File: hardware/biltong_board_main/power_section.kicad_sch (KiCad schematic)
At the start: 17 parts, among them U3 TPS562202SDRLR

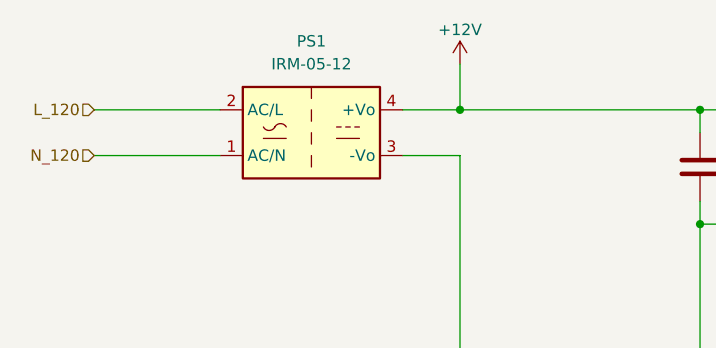
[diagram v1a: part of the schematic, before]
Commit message: generated BOM, swapped 10u cap size, README.md changes
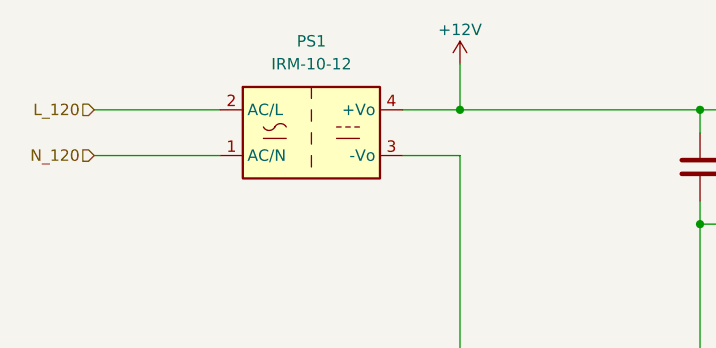
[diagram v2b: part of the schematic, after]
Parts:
- removed PS1: IRM-05-12, BiltongBoardLib:Converter_ACDC_MeanWell_IRM-05-xx_THT_w_model, symbol Converter_ACDC:IRM-05-12
- added PS1: IRM-10-12, BiltongBoardLib:Converter_ACDC_MeanWell_IRM-10-xx_THT_w_model, symbol Converter_ACDC:IRM-10-12
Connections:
- net +12V: now also PS1.4 (+Vo)
- net GND: now also PS1.3 (-Vo)
- net L_120: now also PS1.2 (AC/L)
- net N_120: now also PS1.1 (AC/N)
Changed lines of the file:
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@@
       (effects (font (size 1.27 1.27)) hide)
     )
-    (property "Datasheet" "~" (at 196.85 122.555 0)
+    (property "Datasheet" "https://www.digikey.com/en/products/detail/w%C3%BCrth-elektronik/150060VS75000/4489906" (at 196.85 122.555 0)
       (effects (font (size 1.27 1.27)) hide)
     )
@@
         (path "/0a1e579b-8207-4868-883c-1f24490f13ce/7102a496-acc8-417b-bbc2-3ab3ed47e45b"
           (reference "C19") (unit 1)
+        )
+      )
+    )
+  )
+  (symbol (lib_id "Converter_ACDC:IRM-10-12") (at 50.8 33.02 0) (unit 1)
+    (in_bom yes) (on_board yes) (dnp no) (fields_autoplaced)
+    (property "Reference" "PS1" (at 50.8 22.86 0)
+      (effects (font (size 1.27 1.27)))
+    )
+    (property "Value" "IRM-10-12" (at 50.8 25.4 0)
+      (effects (font (size 1.27 1.27)))
+    )
+    (property "Footprint" "BiltongBoardLib:Converter_ACDC_MeanWell_IRM-10-xx_THT_w_model" (at 50.8 41.91 0)
+      (effects (font (size 1.27 1.27)) hide)
+    )
+    (property "Datasheet" "https://www.meanwell.com/Upload/PDF/IRM-10/IRM-10-SPEC.PDF" (at 50.8 43.18 0)
+      (effects (font (size 1.27 1.27)) hide)
+    )
+    (pin "1")
+    (pin "2")
+    (pin "3")
+    (pin "4")
+    (instances
+      (project "biltong_board_main"
+        (path "/0a1e579b-8207-4868-883c-1f24490f13ce/7102a496-acc8-417b-bbc2-3ab3ed47e45b"
+          (reference "PS1") (unit 1)
         )
       )
@@
         )
       )
-    )
-  )
-  (symbol (lib_id "Converter_ACDC:IRM-05-12") (at 50.8 33.02 0) (unit 1)
-    (in_bom yes) (on_board yes) (dnp no) (fields_autoplaced)
-    (property "Reference" "PS1" (at 50.8 22.86 0)
-      (effects (font (size 1.27 1.27)))
-    )
-    (property "Value" "IRM-05-12" (at 50.8 25.4 0)
-      (effects (font (size 1.27 1.27)))
-    )
-    (property "Footprint" "BiltongBoardLib:Converter_ACDC_MeanWell_IRM-05-xx_THT_w_model" (at 50.8 41.91 0)
-      (effects (font (size 1.27 1.27)) hide)
-    )
-    (property "Datasheet" "https://www.meanwell.com/Upload/PDF/IRM-05/IRM-05-SPEC.PDF" (at 50.8 43.18 0)
-      (effects (font (size 1.27 1.27)) hide)
-    )
-    (pin "1")
-    (pin "2")
-    (pin "3")
-    (pin "4")
-    (instances
-      (project "biltong_board_main"
-        (path "/0a1e579b-8207-4868-883c-1f24490f13ce/7102a496-acc8-417b-bbc2-3ab3ed47e45b"
-          (reference "PS1") (unit 1)
-        )
-      )

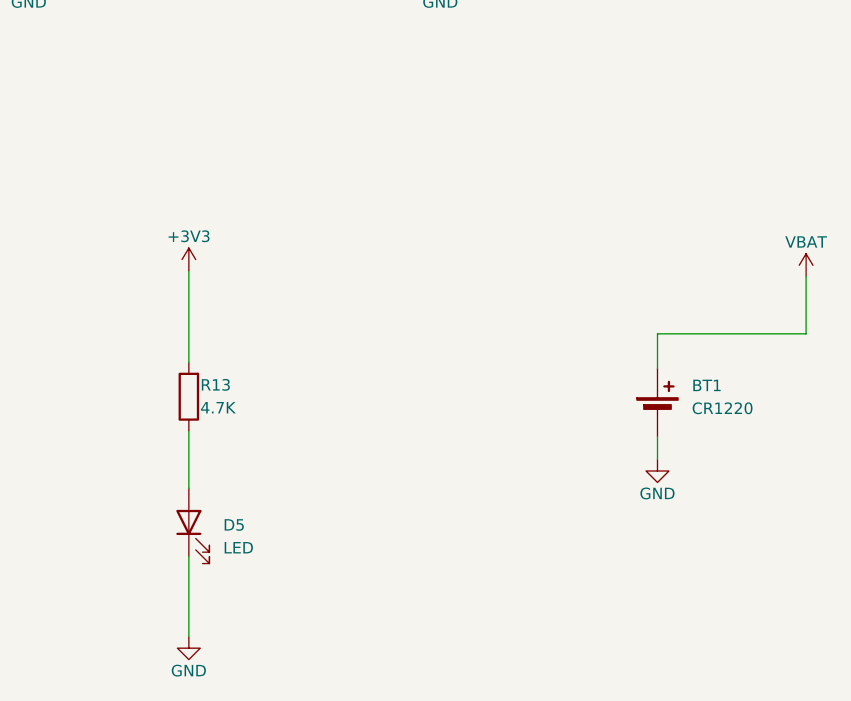
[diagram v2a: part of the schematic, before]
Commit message: Fixed HS1 ground issue, missing schematic values, README.md update
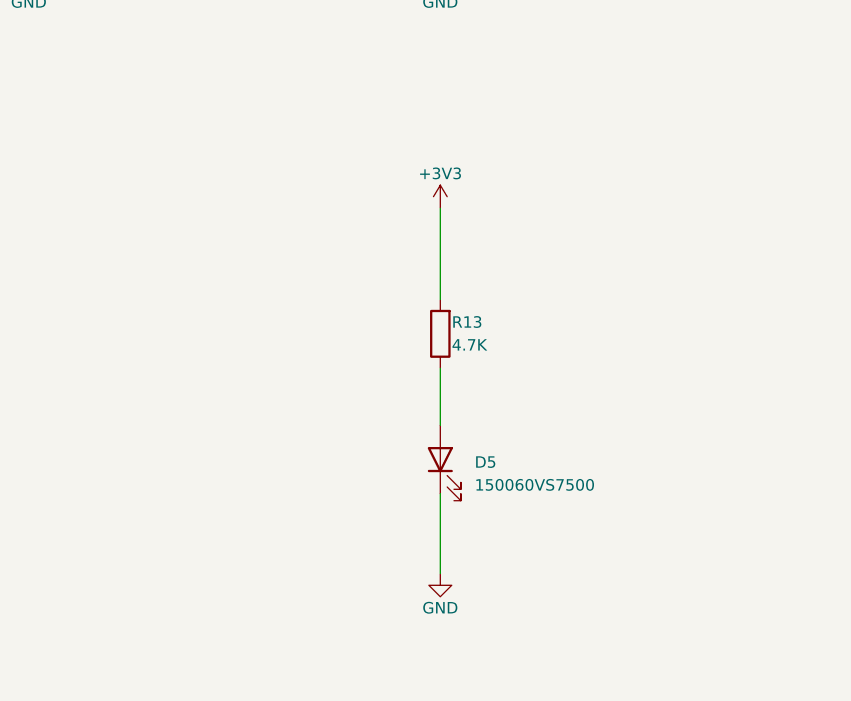
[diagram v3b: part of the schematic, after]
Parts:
- removed BT1: CR1220, BiltongBoardLib:BH-98-1, symbol Device:Battery_Cell
- D5: value LED -> 150060VS7500
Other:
- moved on the sheet: D5, R13
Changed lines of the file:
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@@
   (junction (at 224.79 30.48) (diameter 0) (color 0 0 0 0)
   )
-  (wire (pts (xy 196.85 126.365) (xy 196.85 135.255))
+  (wire (pts (xy 224.79 119.38) (xy 224.79 128.27))
     (stroke (width 0) (type default))
   )
@@
     (stroke (width 0) (type default))
   )
-  (wire (pts (xy 248.92 105.41) (xy 248.92 101.6))
-    (stroke (width 0) (type default))
-  )
   (wire (pts (xy 93.98 40.64) (xy 93.98 43.18))
     (stroke (width 0) (type default))
@@
     (stroke (width 0) (type default))
   )
-  (wire (pts (xy 248.92 113.03) (xy 248.92 115.57))
-    (stroke (width 0) (type default))
-  )
   (wire (pts (xy 203.2 60.96) (xy 195.58 60.96))
     (stroke (width 0) (type default))
@@
     (stroke (width 0) (type default))
   )
-  (wire (pts (xy 265.43 101.6) (xy 265.43 95.25))
-    (stroke (width 0) (type default))
-  )
-  (wire (pts (xy 196.85 112.395) (xy 196.85 118.745))
+  (wire (pts (xy 224.79 105.41) (xy 224.79 111.76))
     (stroke (width 0) (type default))
   )
@@
     (stroke (width 0) (type default))
   )
-  (wire (pts (xy 248.92 101.6) (xy 265.43 101.6))
-    (stroke (width 0) (type default))
-  )
-  (wire (pts (xy 196.85 94.615) (xy 196.85 104.775))
+  (wire (pts (xy 224.79 87.63) (xy 224.79 97.79))
     (stroke (width 0) (type default))
   )
@@
     )
   )
-  (symbol (lib_id "Device:LED") (at 196.85 122.555 90) (unit 1)
+  (symbol (lib_id "Device:LED") (at 224.79 115.57 90) (unit 1)
     (in_bom yes) (on_board yes) (dnp no) (fields_autoplaced)
-    (property "Reference" "D5" (at 200.66 122.8725 90)
+    (property "Reference" "D5" (at 228.6 115.8875 90)
       (effects (font (size 1.27 1.27)) (justify right))
     )
-    (property "Value" "LED" (at 200.66 125.4125 90)
+    (property "Value" "150060VS7500" (at 228.6 118.4275 90)
       (effects (font (size 1.27 1.27)) (justify right))
     )
-    (property "Footprint" "LED_SMD:LED_0603_1608Metric" (at 196.85 122.555 0)
-      (effects (font (size 1.27 1.27)) hide)
-    )
-    (property "Datasheet" "https://www.digikey.com/en/products/detail/w%C3%BCrth-elektronik/150060VS75000/4489906" (at 196.85 122.555 0)
+    (property "Footprint" "LED_SMD:LED_0603_1608Metric" (at 224.79 115.57 0)
+      (effects (font (size 1.27 1.27)) hide)
+    )
+    (property "Datasheet" "https://www.digikey.com/en/products/detail/w%C3%BCrth-elektronik/150060VS75000/4489906" (at 224.79 115.57 0)
       (effects (font (size 1.27 1.27)) hide)
     )
@@
     )
   )
-  (symbol (lib_id "BiltongBoard:VBAT") (at 265.43 95.25 0) (unit 1)
-    (in_bom yes) (on_board yes) (dnp no)
-    (property "Reference" "#PWR048" (at 265.43 87.63 0)
-      (effects (font (size 1.27 1.27)) hide)
-    )
-    (property "Value" "VBAT" (at 265.43 91.44 0)
-      (effects (font (size 1.27 1.27)))
-    )
-    (property "Footprint" "" (at 265.43 95.25 0)
-      (effects (font (size 1.27 1.27)) hide)
-    )
-    (property "Datasheet" "" (at 265.43 95.25 0)
-      (effects (font (size 1.27 1.27)) hide)
-    )
-    (pin "1")
-    (instances
-      (project "biltong_board_main"
-        (path "/0a1e579b-8207-4868-883c-1f24490f13ce/7102a496-acc8-417b-bbc2-3ab3ed47e45b"
-          (reference "#PWR048") (unit 1)
-        )
-      )
-    )
-  )
   (symbol (lib_id "Device:C") (at 207.01 60.96 90) (unit 1)
     (in_bom yes) (on_board yes) (dnp no)
@@
     )
   )
-  (symbol (lib_id "power:+3V3") (at 196.85 94.615 0) (mirror y) (unit 1)
-    (in_bom yes) (on_board yes) (dnp no)
-    (property "Reference" "#PWR032" (at 196.85 98.425 0)
-      (effects (font (size 1.27 1.27)) hide)
-    )
-    (property "Value" "+3V3" (at 196.85 90.805 0)
-      (effects (font (size 1.27 1.27)))
-    )
-    (property "Footprint" "" (at 196.85 94.615 0)
-      (effects (font (size 1.27 1.27)) hide)
-    )
-    (property "Datasheet" "" (at 196.85 94.615 0)
+  (symbol (lib_id "power:+3V3") (at 224.79 87.63 0) (mirror y) (unit 1)
+    (in_bom yes) (on_board yes) (dnp no)
+    (property "Reference" "#PWR032" (at 224.79 91.44 0)
+      (effects (font (size 1.27 1.27)) hide)
+    )
+    (property "Value" "+3V3" (at 224.79 83.82 0)
+      (effects (font (size 1.27 1.27)))
+    )
+    (property "Footprint" "" (at 224.79 87.63 0)
+      (effects (font (size 1.27 1.27)) hide)
+    )
+    (property "Datasheet" "" (at 224.79 87.63 0)
       (effects (font (size 1.27 1.27)) hide)
     )
@@
     )
   )
-  (symbol (lib_id "power:GND") (at 196.85 135.255 0) (mirror y) (unit 1)
-    (in_bom yes) (on_board yes) (dnp no)
-    (property "Reference" "#PWR033" (at 196.85 141.605 0)
-      (effects (font (size 1.27 1.27)) hide)
-    )
-    (property "Value" "GND" (at 196.85 139.065 0)
-      (effects (font (size 1.27 1.27)))
-    )
-    (property "Footprint" "" (at 196.85 135.255 0)
-      (effects (font (size 1.27 1.27)) hide)
-    )
-    (property "Datasheet" "" (at 196.85 135.255 0)
+  (symbol (lib_id "power:GND") (at 224.79 128.27 0) (mirror y) (unit 1)
+    (in_bom yes) (on_board yes) (dnp no)
+    (property "Reference" "#PWR033" (at 224.79 134.62 0)
+      (effects (font (size 1.27 1.27)) hide)
+    )
+    (property "Value" "GND" (at 224.79 132.08 0)
+      (effects (font (size 1.27 1.27)))
+    )
+    (property "Footprint" "" (at 224.79 128.27 0)
+      (effects (font (size 1.27 1.27)) hide)
+    )
+    (property "Datasheet" "" (at 224.79 128.27 0)
       (effects (font (size 1.27 1.27)) hide)
     )
@@
     )
   )
-  (symbol (lib_id "Device:R") (at 196.85 108.585 180) (unit 1)
-    (in_bom yes) (on_board yes) (dnp no)
-    (property "Reference" "R13" (at 198.12 107.315 0)
+  (symbol (lib_id "Device:R") (at 224.79 101.6 180) (unit 1)
+    (in_bom yes) (on_board yes) (dnp no)
+    (property "Reference" "R13" (at 226.06 100.33 0)
       (effects (font (size 1.27 1.27)) (justify right))
     )
-    (property "Value" "4.7K" (at 198.12 109.855 0)
+    (property "Value" "4.7K" (at 226.06 102.87 0)
       (effects (font (size 1.27 1.27)) (justify right))
     )
-    (property "Footprint" "Resistor_SMD:R_0603_1608Metric" (at 198.628 108.585 90)
-      (effects (font (size 1.27 1.27)) hide)
-    )
-    (property "Datasheet" "~" (at 196.85 108.585 0)
+    (property "Footprint" "Resistor_SMD:R_0603_1608Metric" (at 226.568 101.6 90)
+      (effects (font (size 1.27 1.27)) hide)
+    )
+    (property "Datasheet" "~" (at 224.79 101.6 0)
       (effects (font (size 1.27 1.27)) hide)
     )
@@
     )
   )
-  (symbol (lib_id "power:GND") (at 248.92 115.57 0) (unit 1)
-    (in_bom yes) (on_board yes) (dnp no)
-    (property "Reference" "#PWR012" (at 248.92 121.92 0)
-      (effects (font (size 1.27 1.27)) hide)
-    )
-    (property "Value" "GND" (at 248.92 119.38 0)
-      (effects (font (size 1.27 1.27)))
-    )
-    (property "Footprint" "" (at 248.92 115.57 0)
-      (effects (font (size 1.27 1.27)) hide)
-    )
-    (property "Datasheet" "" (at 248.92 115.57 0)
-      (effects (font (size 1.27 1.27)) hide)
-    )
-    (pin "1")
-    (instances
-      (project "biltong_board_main"
-        (path "/0a1e579b-8207-4868-883c-1f24490f13ce"
-          (reference "#PWR012") (unit 1)
-        )
-        (path "/0a1e579b-8207-4868-883c-1f24490f13ce/7102a496-acc8-417b-bbc2-3ab3ed47e45b"
-          (reference "#PWR031") (unit 1)
-        )
-      )
-    )
-  )
   (symbol (lib_id "power:+3V3") (at 265.43 25.4 0) (unit 1)
     (in_bom yes) (on_board yes) (dnp no)
@@
         )
       )
-    )
-  )
-  (symbol (lib_id "Device:Battery_Cell") (at 248.92 110.49 0) (unit 1)
-    (in_bom yes) (on_board yes) (dnp no) (fields_autoplaced)
-    (property "Reference" "BT1" (at 252.73 107.3785 0)
-      (effects (font (size 1.27 1.27)) (justify left))
-    )
-    (property "Value" "CR1220" (at 252.73 109.9185 0)
-      (effects (font (size 1.27 1.27)) (justify left))
-    )
-    (property "Footprint" "BiltongBoardLib:BH-98-1" (at 248.92 108.966 90)
-      (effects (font (size 1.27 1.27)) hide)
-    )
-    (property "Datasheet" "~" (at 248.92 108.966 90)
-      (effects (font (size 1.27 1.27)) hide)
-    )
-    (pin "1")
-    (pin "2")
-    (instances
-      (project "biltong_board_main"
-        (path "/0a1e579b-8207-4868-883c-1f24490f13ce"
-          (reference "BT1") (unit 1)
-        )
-        (path "/0a1e579b-8207-4868-883c-1f24490f13ce/7102a496-acc8-417b-bbc2-3ab3ed47e45b"
-          (reference "BT1") (unit 1)
-        )
-      )
